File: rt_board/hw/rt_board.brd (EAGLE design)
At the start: 100 x 80 mm, 66 parts, among them IC1 MCP170333MB, IC2/L1 TLE4935L, IC3/L2 TLE4935L, IC4/L1 TLE4935L, IC5/L2 TLE4935L, Q1 8MHz, SW1 B3U-1000PM-B, SW2 B3U-1000PM-B, U1 STM32F051R8T7, U2 SN74AVC4T245PW, U3 DRV8801PWP, U4 ACS712ELCTR-05B-T, U5 DRV8801PWP, U6 ACS712ELCTR-05B-T, U7 2N7002BKW, X1 PWR, X2 LEFT, X3 RIGHT

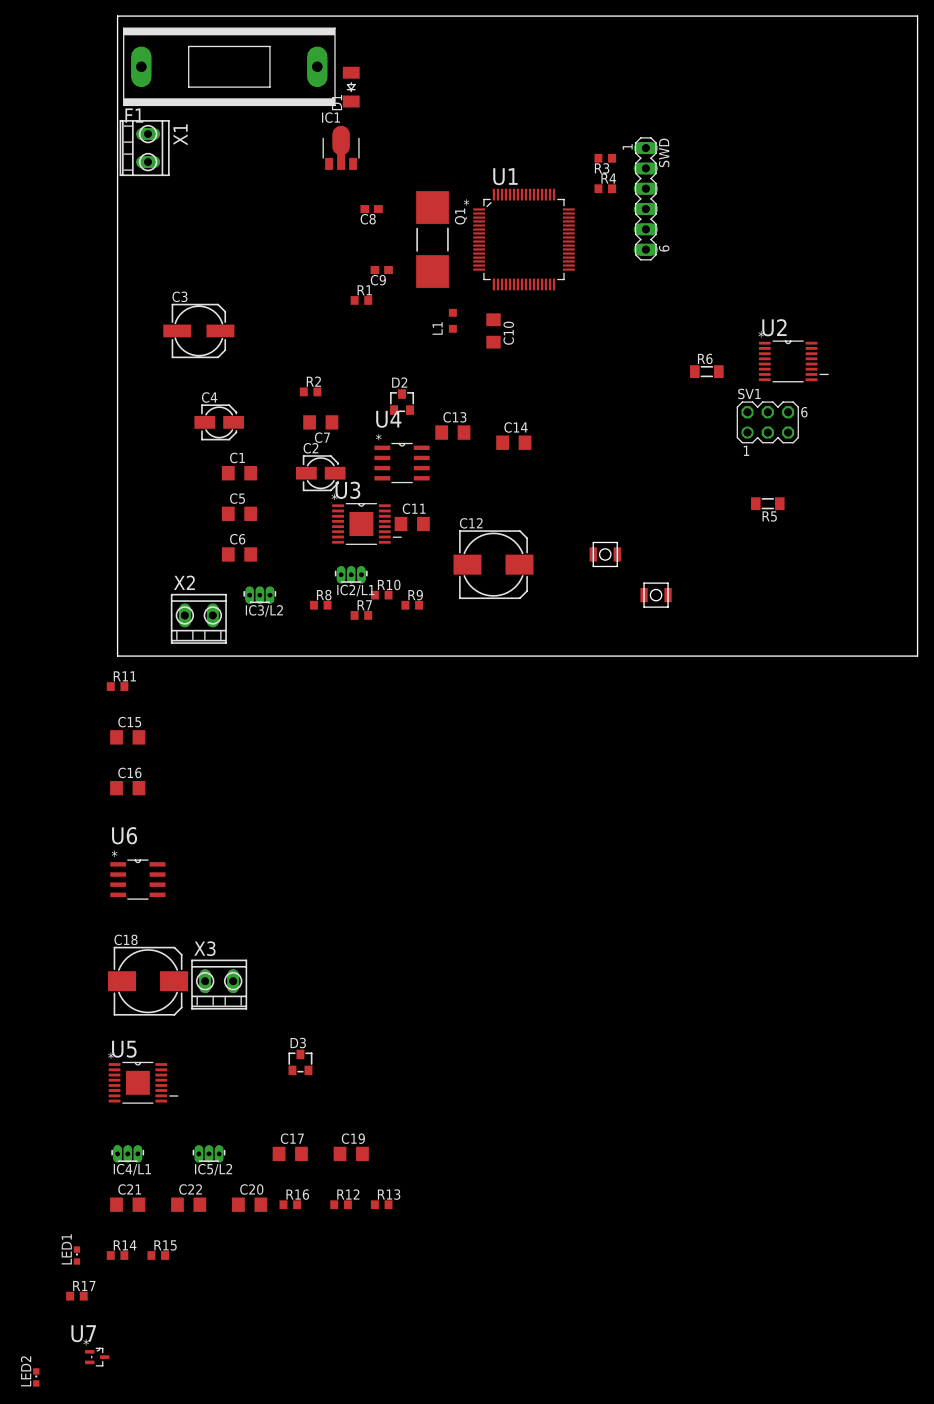
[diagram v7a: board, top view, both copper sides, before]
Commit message: first PCB/SMD version
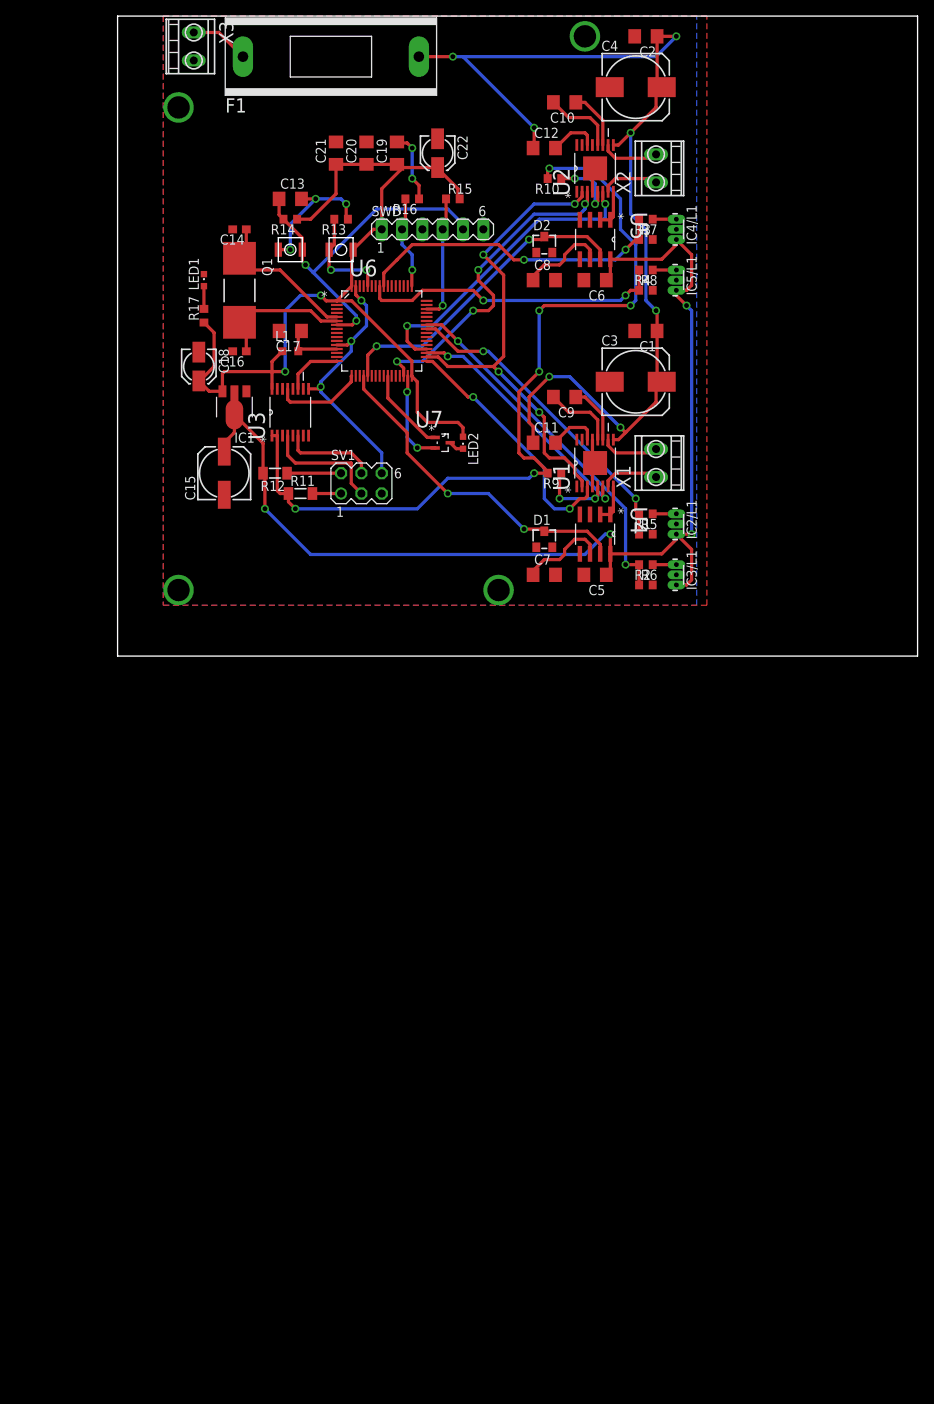
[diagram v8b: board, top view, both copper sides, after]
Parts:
- removed D3: BZX84CSMD, diode:TO236
- removed IC3/L2, IC5/L2: TLE4935L, allegro:SIP3-UA
- added IC3/L1, IC5/L1: TLE4935L, allegro:SIP3-UA
- C12: value 100uF -> 100nF; device rcl:153CLV-0810 -> rcl:C1206
- C14: value 1nF -> 20pF; device rcl:C1206 -> rcl:C0603
- C15: value 100nF -> 100uF; device rcl:C1206 -> rcl:153CLV-0605
- C16: value 100nF -> 20pF; device rcl:C1206 -> rcl:C0603
- C18: value 100uF -> 4.7uF; device rcl:153CLV-0810 -> rcl:153CLV-0405
- C2: value 4.7uF -> 100nF; device rcl:153CLV-0405 -> rcl:C1206
- C20: value 1nF -> 100nF
- C22: value 100nF -> 4.7uF; device rcl:C1206 -> rcl:153CLV-0405
- C3: device rcl:153CLV-0605 -> rcl:153CLV-0810
- C4: value 4.7uF -> 100uF; device rcl:153CLV-0405 -> rcl:153CLV-0810
- C7: value 100nF -> 1nF
- C8: value 20pF -> 1nF; device rcl:C0603 -> rcl:C1206
- C9: value 20pF -> 100nF; device rcl:C0603 -> rcl:C1206
- D1: value CGRM4001-G -> BZX84CSMD; device diode:SOD-123_MINI-SMA -> diode:TO236
- R1, R2: value 1kR -> 2kR
- R10: value 3kR -> 3.3kR
- R11: value 3.3kR -> 350mA; device rcl:R0603 -> rcl:MINI_MELF-0204W
- R12: value 2kR -> 350mA; device rcl:R0603 -> rcl:MINI_MELF-0204W
- R13: value 3kR -> 1kR
- R14: value 2kR -> 1kR
- R15: value 3kR -> 100kR
- R16: value 3.3kR -> 100kR
- R3, R4: value 100kR -> 2kR
- R5, R6: value 350mA -> 3kR; device rcl:MINI_MELF-0204W -> rcl:R0603
- R7: value 2kR -> 3kR
- R9: value 2kR -> 3.3kR
- U1: value STM32F051R8T7 -> DRV8801PWP; device stm32f51r8r6:QFP50P1200X1200X160-64N -> TI-DRV8801PWP:SOP65P640X120-17N
- U2: value SN74AVC4T245PW -> DRV8801PWP; device TI-SN74AVC4T245PW:SOP65P640X120-16N -> TI-DRV8801PWP:SOP65P640X120-17N
- U3: value DRV8801PWP -> SN74AVC4T245PW; device TI-DRV8801PWP:SOP65P640X120-17N -> TI-SN74AVC4T245PW:SOP65P640X120-16N
- U5: value DRV8801PWP -> ACS712ELCTR-05B-T; device TI-DRV8801PWP:SOP65P640X120-17N -> Allegro-ACS712ELCTR-20A-T:SOIC127P600X175-8N
- U6: value ACS712ELCTR-05B-T -> STM32F051R8T7; device Allegro-ACS712ELCTR-20A-T:SOIC127P600X175-8N -> stm32f51r8r6:QFP50P1200X1200X160-64N
- X1: value PWR -> LEFT
- X2: value LEFT -> RIGHT
- X3: value RIGHT -> PWR
- moved R15 137.1 mm to (41.9, 57.1)
- moved C22 135.1 mm to (40.0, 62.9), turned to 270 degrees
- moved IC4/L1 134.4 mm to (69.8, 53.3), turned to 90 degrees
- moved C21 134.0 mm to (27.3, 62.9), turned to 90 degrees
- moved C20 132.3 mm to (31.1, 62.9), turned to 90 degrees
- moved R14 131.3 mm to (21.6, 54.6), turned to 180 degrees
- moved LED2 128.4 mm to (43.2, 26.7), turned to 180 degrees
- moved R16 126.7 mm to (36.8, 57.1), turned to 180 degrees
- moved C19 125.2 mm to (34.9, 62.9), turned to 90 degrees
- moved R17 123.6 mm to (10.8, 42.5), turned to 90 degrees
- moved R13 123.3 mm to (27.9, 54.6), turned to 180 degrees
- moved LED1 122.9 mm to (10.8, 47.0)
- moved U7 122.2 mm to (40.6, 26.7)
- moved U5 119.9 mm to (59.7, 52.1), turned to 270 degrees
- moved X3 116.9 mm to (9.53, 76.2), turned to 270 degrees
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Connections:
- removed net N$1: C3.+, D1.C, IC1.2@1
- net +12V: now also C1.1, C12.1, C2.1, C3.+, C4.+, U1.9, U2.9; no longer C12.+, C15.1, C17.1, C18.+, C21.1, U3.9, U5.9
- net +5V: now also C18.+, C19.1, C20.1, C21.1, C22.+, R14.1, R15.2, U3.16, U6.1, U6.32, U6.64; no longer C1.1, C2.+, C4.+, C5.1, C6.1, R2.1, R4.2, U1.1, U1.32, U1.64, U2.16
- net +5V/1: now also C15.+, C5.1, C6.1, IC1.2@1, IC3/L1.1, IC5/L1.1, R12.2, U5.8; no longer C13.1, C19.1, D1.A, IC3/L2.1, IC5/L2.1, R6.2, U6.8
- net +5V/4: now also R10.2, R11.1, R9.2, U3.1, U3.2; no longer R11.2, R16.2, R5.1, U2.1, U2.2
- net 0V: now also C15.-, C16.2, C2.2, C21.2, C22.-, D1.A, IC3/L1.2, IC5/L1.2, R13.1, R16.1, R5.2, R6.2, R7.2, U1.13, U1.16, U1.17, U1.4, U2.13, U2.16, U2.17, U2.4, U3.14, U3.15, U3.3, U3.8, U3.9, U5.3, U5.5, U6.12, U6.31, U6.63, X3.2; no longer C10.2, C11.2, C12.-, C2.-, C9.2, D3.A, IC3/L2.2, IC5/L2.2, R1.1, R10.2, R13.2, R15.2, R3.1, U1.12, U1.31, U1.63, U2.14, U2.15, U2.3, U2.8, U2.9, U3.13, U3.16, U3.17, U3.4, U5.13, U5.16, U5.17, U6.3, U6.4, U6.5, X1.2
- net N$10: now also R12.1; no longer R6.1
- net N$11: now also R11.2; no longer R5.2
- net N$12: now also U3.4; no longer U2.4
- net N$13: now also U3.13, U6.17; no longer U1.17, U2.13
- net N$14: now also U3.11, U6.16; no longer U1.16, U2.11
- net N$15: now also U3.6; no longer U2.6
- net N$16: now also R1.1; no longer R7.1
- net N$17: now also R1.2, R5.1, U6.41; no longer R7.2, R8.1, U1.41
- net N$18: now also IC3/L1.3, R2.1; no longer IC3/L2.3, R9.1
- net N$19: now also R2.2, R6.1, U6.42; no longer R10.1, R9.2, U1.42
- net N$2: now also X3.1; no longer X1.1
- net N$20: now also U1.7, X1.1; no longer U3.7, X2.1
- net N$21: now also U1.10, X1.2; no longer U3.10, X2.2
- net N$22: now also U1.8; no longer U3.8
- net N$23: now also D1.C, U6.20; no longer D2.C, U1.20
- net N$24: now also C7.1; no longer C14.1
- net N$25: now also R9.1, U1.5; no longer R11.1, U3.5
- net N$26: now also C11.2, U1.14; no longer C15.2, U3.14
- net N$27: now also C9.2, U1.12; no longer C16.2, U3.12
- net N$28: now also C9.1, U1.11; no longer C16.1, U3.11
- net N$29: now also R3.1; no longer R12.1
- net N$3: now also C17.1, U6.13; no longer C10.1, U1.13
- net N$30: now also R3.2, R7.1, U6.56; no longer R12.2, R13.1, U1.56
- net N$31: now also IC5/L1.3, R4.1; no longer IC5/L2.3, R14.1
- net N$32: now also R4.2, R8.1, U6.57; no longer R14.2, R15.1, U1.57
- net N$33: now also U2.7, X2.1; no longer U5.7, X3.1
- net N$34: now also U2.10, X2.2; no longer U5.10, X3.2
- net N$35: now also C8.1, U5.6; no longer C20.1, U6.6
- net N$36: now also U2.8, U5.1, U5.2; no longer U5.8, U6.1, U6.2
- net N$37: now also D2.C, U5.7, U6.21; no longer D3.C, U1.21, U6.7
- net N$38: now also R10.1, U2.5; no longer R16.1, U5.5
- net N$39: now also C12.2, U2.14; no longer C21.2, U5.14
- net N$4: now also R16.2, U6.49; no longer R3.2, U1.49
- net N$40: now also C10.2, U2.12; no longer C22.2, U5.12
- net N$41: now also C10.1, U2.11; no longer C22.1, U5.11
- net N$42: now also U1.2, U2.2, U6.34; no longer U1.34, U3.2, U5.2
- net N$44: now also U6.26; no longer U1.26
- net N$45: now also U1.6, U6.35; no longer U1.35, U3.6
- net N$46: now also U2.6, U6.36; no longer U1.36, U5.6
- net N$48: now also U1.3, U6.33; no longer U1.33, U3.3
- net N$49: now also U2.3, U6.30; no longer U1.30, U5.3
- net N$5: now also R13.2, U6.60; no longer R1.2, U1.60
- net N$6: now also C13.1, R14.2, U6.7; no longer C7.1, R2.2, U1.7
- net N$7: now also C14.1, U6.5; no longer C8.1, U1.5
- net N$8: now also C16.1, U6.6; no longer C9.1, U1.6
- net N$9: now also R15.1, U6.46; no longer R4.1, U1.46
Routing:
- net +5V/1: track 0.00 -> 143.0 mm, vias 0 -> 4
- net +12V: track 0.00 -> 133.0 mm, vias 0 -> 7
- net +5V: track 0.00 -> 117.9 mm, vias 0 -> 2
- net +5V/4: track 0.00 -> 106.2 mm, vias 0 -> 6
- net 0V: track 0.00 -> 80.0 mm, vias 0 -> 10
- net N$42: track 0.00 -> 61.1 mm, vias 0 -> 4
- net N$19: track 0.00 -> 45.6 mm, vias 0 -> 2
- net N$6: track 0.00 -> 45.3 mm, vias 0 -> 2
- net N$23: track 0.00 -> 41.9 mm, vias 0 -> 2
- net N$49: track 0.00 -> 41.1 mm, vias 0 -> 4
- net N$37: track 0.00 -> 39.7 mm, vias 0 -> 2
- net N$17: track 0.00 -> 39.5 mm, vias 0 -> 2
- net N$30: track 0.00 -> 39.4 mm, vias 0 -> 2
- net N$46: track 0.00 -> 38.6 mm, vias 0 -> 2
- net N$32: track 0.00 -> 38.2 mm, vias 0 -> 2
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- added copper zone on layer 1, net 0V
- added copper zone on layer 16, net N$50
